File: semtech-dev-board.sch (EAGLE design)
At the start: 58 parts, among them Q1 BSS123, U1 SEMTECH_SX1236, U3 MIC5219 3.3V, X1 BU-SMA-G, X2 BU-SMA-G, X3 BU-SMA-G, X4 BU-SMA-G

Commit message: Fixed inductors
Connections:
- net N$10 renamed DIO2
- net N$11 renamed DIO3
- net N$12 renamed DIO4
- net N$13 renamed DIO5
- net N$17 renamed RFO_LF_PA
- net N$19 renamed RFO_HF_PA
- net N$22 renamed RFO_HF_1
- net N$23 renamed RFO_HF_2
- net N$26 renamed RFO_LF_1
- net N$27 renamed RFO_LF_2
- net N$28 renamed RFO_LF_OUT
- net N$4 renamed RST_SUP
- net N$5 renamed DIO0
- net N$9 renamed DIO1
- removed net N$14: C4.1, U1.VR_ANA
- removed net SPI_MOSI: JP2.2, U1.MOSI
- removed net SPI_SCK: JP2.3, U1.SCK
- new net N$4: JP2.2, U1.MISO
- new net N$5: JP2.1, U1.SCK
- net N$3: now also JP2.3, U1.MOSI; no longer JP2.1, U1.MISO
- net VR_ANA: now also C4.1, U1.VR_ANA; no longer U1.VR_DIG
- net VR_DIG: now also U1.VR_DIG
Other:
- moved on the sheet: L1, L2, L4, L5, L6, L7, L8
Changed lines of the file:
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@@
 <layers>
 <layer number="1" name="Top" color="4" fill="1" visible="no" active="no"/>
+<layer number="2" name="Route2" color="1" fill="3" visible="no" active="no"/>
+<layer number="3" name="Route3" color="4" fill="3" visible="no" active="no"/>
+<layer number="4" name="Route4" color="1" fill="4" visible="no" active="no"/>
+<layer number="5" name="Route5" color="4" fill="4" visible="no" active="no"/>
+<layer number="6" name="Route6" color="1" fill="8" visible="no" active="no"/>
+<layer number="7" name="Route7" color="4" fill="8" visible="no" active="no"/>
+<layer number="8" name="Route8" color="1" fill="2" visible="no" active="no"/>
+<layer number="9" name="Route9" color="4" fill="2" visible="no" active="no"/>
+<layer number="10" name="Route10" color="1" fill="7" visible="no" active="no"/>
+<layer number="11" name="Route11" color="4" fill="7" visible="no" active="no"/>
+<layer number="12" name="Route12" color="1" fill="5" visible="no" active="no"/>
+<layer number="13" name="Route13" color="4" fill="5" visible="no" active="no"/>
+<layer number="14" name="Route14" color="1" fill="6" visible="no" active="no"/>
+<layer number="15" name="Route15" color="4" fill="6" visible="no" active="no"/>
 <layer number="16" name="Bottom" color="1" fill="1" visible="no" active="no"/>
 <layer number="17" name="Pads" color="2" fill="1" visible="no" active="no"/>
@@
 <instance part="C8" gate="G$1" x="127" y="127"/>
 <instance part="L3" gate="G$1" x="149.86" y="119.38" rot="R180"/>
-<instance part="L1" gate="G$1" x="139.7" y="132.08" rot="R270"/>
+<instance part="L1" gate="G$1" x="139.7" y="132.08" rot="MR90"/>
 <instance part="C10" gate="G$1" x="154.94" y="127"/>
 <instance part="C11" gate="G$1" x="162.56" y="137.16" rot="R90"/>
-<instance part="L5" gate="G$1" x="180.34" y="137.16" rot="R270"/>
-<instance part="L7" gate="G$1" x="203.2" y="137.16" rot="R270"/>
+<instance part="L5" gate="G$1" x="180.34" y="137.16" rot="MR90"/>
+<instance part="L7" gate="G$1" x="203.2" y="137.16" rot="MR90"/>
 <instance part="C14" gate="G$1" x="177.8" y="144.78" rot="R90"/>
 <instance part="C17" gate="G$1" x="200.66" y="144.78" rot="R90"/>
@@
 <instance part="C12" gate="G$1" x="165.1" y="83.82"/>
 <instance part="C13" gate="G$1" x="175.26" y="93.98" rot="R90"/>
-<instance part="L6" gate="G$1" x="193.04" y="93.98" rot="R270"/>
-<instance part="L8" gate="G$1" x="215.9" y="93.98" rot="R270"/>
+<instance part="L6" gate="G$1" x="193.04" y="93.98" rot="MR90"/>
+<instance part="L8" gate="G$1" x="215.9" y="93.98" rot="MR90"/>
 <instance part="C15" gate="G$1" x="190.5" y="101.6" rot="R90"/>
 <instance part="C19" gate="G$1" x="213.36" y="101.6" rot="R90"/>
 <instance part="C18" gate="G$1" x="205.74" y="88.9"/>
 <instance part="C22" gate="G$1" x="228.6" y="88.9"/>
-<instance part="L4" gate="G$1" x="157.48" y="76.2"/>
-<instance part="L2" gate="G$1" x="139.7" y="93.98" rot="R270"/>
+<instance part="L4" gate="G$1" x="157.48" y="76.2" rot="MR0"/>
+<instance part="L2" gate="G$1" x="139.7" y="93.98" rot="MR90"/>
 <instance part="C9" gate="G$1" x="127" y="88.9"/>
 <instance part="AGND3" gate="VR1" x="127" y="116.84" rot="MR0"/>
@@
 </segment>
 </net>
-<net name="SPI_SCK" class="0">
-<segment>
-<pinref part="U1" gate="G$1" pin="SCK"/>
-<wire x1="48.26" y1="35.56" x2="40.64" y2="35.56" width="0.1524" layer="91"/>
-<wire x1="40.64" y1="35.56" x2="40.64" y2="30.48" width="0.1524" layer="91"/>
-<wire x1="40.64" y1="30.48" x2="7.62" y2="30.48" width="0.1524" layer="91"/>
-<pinref part="JP2" gate="A" pin="3"/>
-</segment>
-</net>
-<net name="SPI_MOSI" class="0">
-<segment>
-<pinref part="U1" gate="G$1" pin="MOSI"/>
-<wire x1="48.26" y1="38.1" x2="38.1" y2="38.1" width="0.1524" layer="91"/>
-<wire x1="38.1" y1="38.1" x2="38.1" y2="33.02" width="0.1524" layer="91"/>
-<wire x1="38.1" y1="33.02" x2="7.62" y2="33.02" width="0.1524" layer="91"/>
-<pinref part="JP2" gate="A" pin="2"/>
-</segment>
-</net>
 <net name="RFI_HF" class="0">
 <segment>
@@
 </segment>
 </net>
-<net name="VR_ANA" class="0">
+<net name="VR_DIG" class="0">
 <segment>
 <pinref part="U1" gate="G$1" pin="VR_DIG"/>
 <wire x1="60.96" y1="86.36" x2="60.96" y2="91.44" width="0.1524" layer="91"/>
 <wire x1="60.96" y1="91.44" x2="101.6" y2="91.44" width="0.1524" layer="91"/>
-<wire x1="101.6" y1="91.44" x2="101.6" y2="83.82" width="0.1524" layer="91"/>
-</segment>
-</net>
-<net name="VR_DIG" class="0">
-<segment>
 <pinref part="C5" gate="G$1" pin="1"/>
-<wire x1="101.6" y1="86.36" x2="101.6" y2="83.82" width="0.1524" layer="91"/>
+<wire x1="101.6" y1="86.36" x2="101.6" y2="91.44" width="0.1524" layer="91"/>
 </segment>
 </net>
@@
 </segment>
 </net>
-<net name="N$3" class="0">
-<segment>
-<pinref part="U1" gate="G$1" pin="MISO"/>
-<wire x1="48.26" y1="40.64" x2="35.56" y2="40.64" width="0.1524" layer="91"/>
-<wire x1="35.56" y1="40.64" x2="35.56" y2="35.56" width="0.1524" layer="91"/>
-<wire x1="35.56" y1="35.56" x2="7.62" y2="35.56" width="0.1524" layer="91"/>
-<pinref part="JP2" gate="A" pin="1"/>
-</segment>
-</net>
-<net name="N$4" class="0">
+<net name="RST_SUP" class="0">
 <segment>
 <pinref part="S1" gate="G$1" pin="A"/>
@@
 </segment>
 </net>
-<net name="N$5" class="0">
+<net name="DIO0" class="0">
 <segment>
 <pinref part="U1" gate="G$1" pin="DIO0"/>
@@
 </segment>
 </net>
-<net name="N$9" class="0">
+<net name="DIO1" class="0">
 <segment>
 <pinref part="JP1" gate="A" pin="3"/>
@@
 </segment>
 </net>
-<net name="N$10" class="0">
+<net name="DIO2" class="0">
 <segment>
 <pinref part="U1" gate="G$1" pin="DIO2/DATA"/>
@@
 </segment>
 </net>
-<net name="N$11" class="0">
+<net name="DIO3" class="0">
 <segment>
 <pinref part="JP1" gate="A" pin="5"/>
@@
 </segment>
 </net>
-<net name="N$12" class="0">
+<net name="DIO4" class="0">
 <segment>
 <pinref part="U1" gate="G$1" pin="DIO4"/>
@@
 </segment>
 </net>
-<net name="N$13" class="0">
+<net name="DIO5" class="0">
 <segment>
 <pinref part="JP1" gate="A" pin="7"/>
@@
 </segment>
 </net>
-<net name="N$14" class="0">
+<net name="VR_ANA" class="0">
 <segment>
 <pinref part="U1" gate="G$1" pin="VR_ANA"/>
@@
 </segment>
 </net>
-<net name="N$17" class="0">
+<net name="RFO_LF_PA" class="0">
 <segment>
 <pinref part="L3" gate="G$1" pin="2"/>
@@
 </segment>
 </net>
-<net name="N$19" class="0">
+<net name="RFO_HF_PA" class="0">
 <segment>
 <wire x1="157.48" y1="93.98" x2="172.72" y2="93.98" width="0.1524" layer="91"/>
@@
 </segment>
 </net>
-<net name="N$22" class="0">
+<net name="RFO_HF_1" class="0">
 <segment>
 <pinref part="C13" gate="G$1" pin="2"/>
@@
 </segment>
 </net>
-<net name="N$23" class="0">
+<net name="RFO_HF_2" class="0">
 <segment>
 <pinref part="L6" gate="G$1" pin="1"/>
@@
 </segment>
 </net>
-<net name="N$26" class="0">
+<net name="RFO_LF_1" class="0">
 <segment>
 <pinref part="C11" gate="G$1" pin="2"/>
@@
 </segment>
 </net>
-<net name="N$27" class="0">
+<net name="RFO_LF_2" class="0">
 <segment>
 <pinref part="L5" gate="G$1" pin="1"/>
@@
 </segment>
 </net>
-<net name="N$28" class="0">
+<net name="RFO_LF_OUT" class="0">
 <segment>
 <pinref part="L7" gate="G$1" pin="1"/>
@@
 </segment>
 </net>
+<net name="N$3" class="0">
+<segment>
+<pinref part="U1" gate="G$1" pin="MOSI"/>
+<wire x1="48.26" y1="35.56" x2="40.64" y2="35.56" width="0.1524" layer="91"/>
+<wire x1="40.64" y1="35.56" x2="40.64" y2="30.48" width="0.1524" layer="91"/>
+<pinref part="JP2" gate="A" pin="3"/>
+<wire x1="40.64" y1="30.48" x2="7.62" y2="30.48" width="0.1524" layer="91"/>
+</segment>
+</net>
+<net name="N$4" class="0">
+<segment>
+<pinref part="U1" gate="G$1" pin="MISO"/>
+<wire x1="48.26" y1="38.1" x2="38.1" y2="38.1" width="0.1524" layer="91"/>
+<wire x1="38.1" y1="38.1" x2="38.1" y2="33.02" width="0.1524" layer="91"/>
+<pinref part="JP2" gate="A" pin="2"/>
+<wire x1="38.1" y1="33.02" x2="7.62" y2="33.02" width="0.1524" layer="91"/>
+</segment>
+</net>
+<net name="N$5" class="0">
+<segment>
+<pinref part="U1" gate="G$1" pin="SCK"/>
+<wire x1="48.26" y1="40.64" x2="35.56" y2="40.64" width="0.1524" layer="91"/>
+<wire x1="35.56" y1="40.64" x2="35.56" y2="35.56" width="0.1524" layer="91"/>
+<pinref part="JP2" gate="A" pin="1"/>
+<wire x1="35.56" y1="35.56" x2="7.62" y2="35.56" width="0.1524" layer="91"/>
+</segment>
+</net>

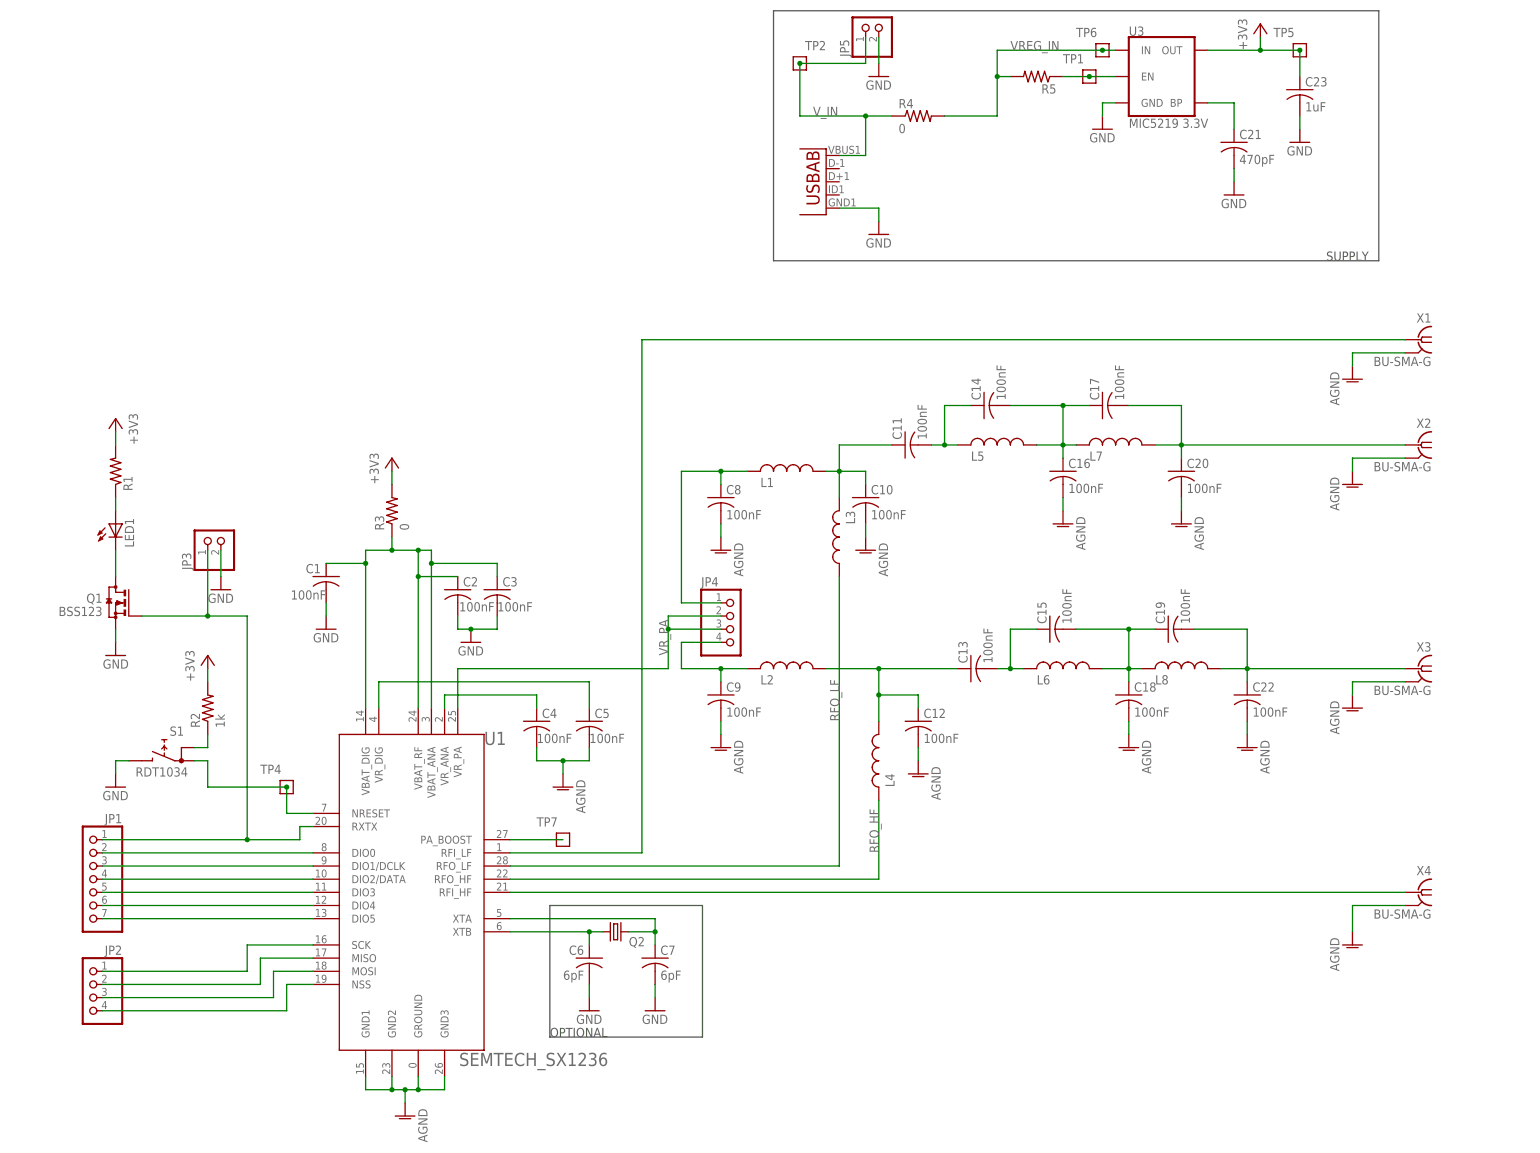
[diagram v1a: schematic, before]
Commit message: Draft arrangement of components
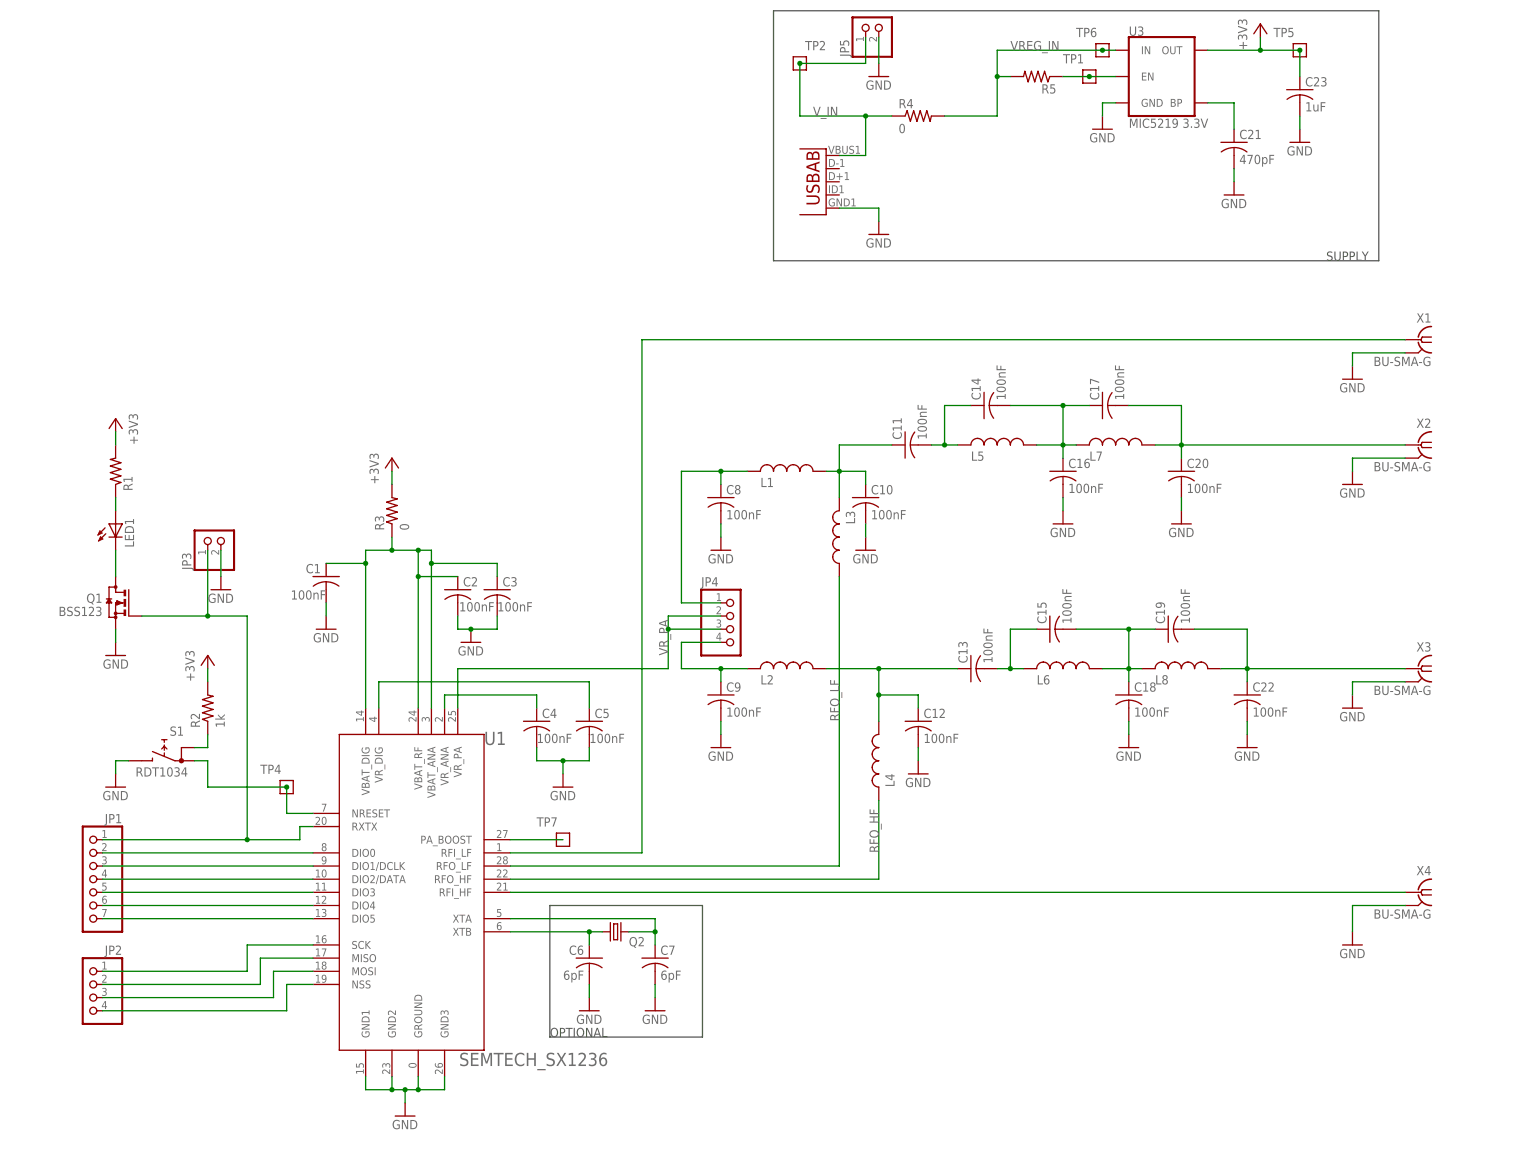
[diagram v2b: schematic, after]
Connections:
- net N$3 renamed SPI_MOSI
- net N$4 renamed SPI_MISO
- net N$5 renamed SPI_SCK
- removed net AGND: C10.2, C12.2, C16.2, C18.2, C20.2, C22.2, C4.2, C5.2, C8.2, C9.2, U1.GND1, U1.GND2, U1.GND3, U1.GROUND, X1.2, X2.2, X3.2, X4.2
- net GND: now also C10.2, C12.2, C16.2, C18.2, C20.2, C22.2, C4.2, C5.2, C8.2, C9.2, U1.GND1, U1.GND2, U1.GND3, U1.GROUND, X1.2, X2.2, X3.2, X4.2
